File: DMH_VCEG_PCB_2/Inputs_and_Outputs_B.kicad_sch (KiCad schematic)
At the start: 34 parts, among them J11 TS_Jack_6.35mm_Sw, J12 TS_Jack_6.35mm_Sw, J13 TS_Jack_6.35mm_Sw, J14 TS_Jack_6.35mm_Sw, J15 TS_Jack_6.35mm_Sw, J16 TS_Jack_6.35mm_Sw, J17 TS_Jack_6.35mm_Sw, J18 TS_Jack_6.35mm_Sw, J19 TS_Jack_6.35mm_Sw, J20 TS_Jack_6.35mm_Sw, J24 Conn_01x10_PinHeader, J25 Conn_01x10_PinHeader, J26 Conn_01x10_PinHeader, J27 Conn_01x06_PinHeader, U18 TL074, U21 TL072

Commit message: Placed ICs and pin headers on PCB 2
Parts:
- J24, J25, J26: footprint Connector_PinHeader_2.54mm:PinHeader_1x10_P2.54mm_Vertical -> Connector_PinSocket_2.54mm:PinSocket_1x10_P2.54mm_Vertical
- J27: footprint (none) -> Connector_PinSocket_2.54mm:PinSocket_1x06_P2.54mm_Vertical
- U21: footprint Package_DIP:DIP-8_W7.62mm -> Package_DIP:DIP-8_W7.62mm_Socket
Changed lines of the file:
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@@
 			)
 		)
-		(property "Footprint" "Connector_PinHeader_2.54mm:PinHeader_1x10_P2.54mm_Vertical"
+		(property "Footprint" "Connector_PinSocket_2.54mm:PinSocket_1x10_P2.54mm_Vertical"
 			(at 144.78 124.46 0)
 			(effects
@@
 			)
 		)
-		(property "Footprint" "Connector_PinHeader_2.54mm:PinHeader_1x10_P2.54mm_Vertical"
+		(property "Footprint" "Connector_PinSocket_2.54mm:PinSocket_1x10_P2.54mm_Vertical"
 			(at 81.28 26.67 0)
 			(effects
@@
 			)
 		)
-		(property "Footprint" "Connector_PinHeader_2.54mm:PinHeader_1x10_P2.54mm_Vertical"
+		(property "Footprint" "Connector_PinSocket_2.54mm:PinSocket_1x10_P2.54mm_Vertical"
 			(at 190.5 151.13 0)
 			(effects
@@
 			)
 		)
-		(property "Footprint" "Connector_PinHeader_2.54mm:PinHeader_1x10_P2.54mm_Vertical"
+		(property "Footprint" "Connector_PinSocket_2.54mm:PinSocket_1x10_P2.54mm_Vertical"
 			(at 190.5 153.67 0)
 			(effects
@@
 			)
 		)
-		(property "Footprint" ""
+		(property "Footprint" "Connector_PinSocket_2.54mm:PinSocket_1x06_P2.54mm_Vertical"
 			(at 107.95 223.52 0)
 			(effects
@@
 			)
 		)
-		(property "Footprint" "Connector_PinHeader_2.54mm:PinHeader_1x10_P2.54mm_Vertical"
+		(property "Footprint" "Connector_PinSocket_2.54mm:PinSocket_1x10_P2.54mm_Vertical"
 			(at 190.5 166.37 0)
 			(effects
@@
 			)
 		)
-		(property "Footprint" "Connector_PinHeader_2.54mm:PinHeader_1x10_P2.54mm_Vertical"
+		(property "Footprint" "Connector_PinSocket_2.54mm:PinSocket_1x10_P2.54mm_Vertical"
 			(at 190.5 163.83 0)
 			(effects
@@
 			)
 		)
-		(property "Footprint" "Connector_PinHeader_2.54mm:PinHeader_1x10_P2.54mm_Vertical"
+		(property "Footprint" "Connector_PinSocket_2.54mm:PinSocket_1x10_P2.54mm_Vertical"
 			(at 190.5 176.53 0)
 			(effects
@@
 			)
 		)
-		(property "Footprint" ""
+		(property "Footprint" "Connector_PinSocket_2.54mm:PinSocket_1x06_P2.54mm_Vertical"
 			(at 177.8 220.98 0)
 			(effects
@@
 			)
 		)
-		(property "Footprint" "Package_DIP:DIP-8_W7.62mm"
+		(property "Footprint" "Package_DIP:DIP-8_W7.62mm_Socket"
 			(at 146.05 228.6 0)
 			(effects
@@
 			)
 		)
-		(property "Footprint" "Connector_PinHeader_2.54mm:PinHeader_1x10_P2.54mm_Vertical"
+		(property "Footprint" "Connector_PinSocket_2.54mm:PinSocket_1x10_P2.54mm_Vertical"
 			(at 144.78 92.71 0)
 			(effects
@@
 			)
 		)
-		(property "Footprint" "Connector_PinHeader_2.54mm:PinHeader_1x10_P2.54mm_Vertical"
+		(property "Footprint" "Connector_PinSocket_2.54mm:PinSocket_1x10_P2.54mm_Vertical"
 			(at 190.5 179.07 0)
 			(effects
@@
 			)
 		)
-		(property "Footprint" "Connector_PinHeader_2.54mm:PinHeader_1x10_P2.54mm_Vertical"
+		(property "Footprint" "Connector_PinSocket_2.54mm:PinSocket_1x10_P2.54mm_Vertical"
 			(at 81.28 58.42 0)
 			(effects
@@
 			)
 		)
-		(property "Footprint" "Connector_PinHeader_2.54mm:PinHeader_1x10_P2.54mm_Vertical"
+		(property "Footprint" "Connector_PinSocket_2.54mm:PinSocket_1x10_P2.54mm_Vertical"
 			(at 81.28 90.17 0)
 			(effects
@@
 			)
 		)
-		(property "Footprint" "Connector_PinHeader_2.54mm:PinHeader_1x10_P2.54mm_Vertical"
+		(property "Footprint" "Connector_PinSocket_2.54mm:PinSocket_1x10_P2.54mm_Vertical"
 			(at 81.28 119.38 0)
 			(effects
@@
 			)
 		)
-		(property "Footprint" "Connector_PinHeader_2.54mm:PinHeader_1x10_P2.54mm_Vertical"
+		(property "Footprint" "Connector_PinSocket_2.54mm:PinSocket_1x10_P2.54mm_Vertical"
 			(at 144.78 29.21 0)
 			(effects
@@
 			)
 		)
-		(property "Footprint" "Connector_PinHeader_2.54mm:PinHeader_1x10_P2.54mm_Vertical"
+		(property "Footprint" "Connector_PinSocket_2.54mm:PinSocket_1x10_P2.54mm_Vertical"
 			(at 144.78 60.96 0)
 			(effects

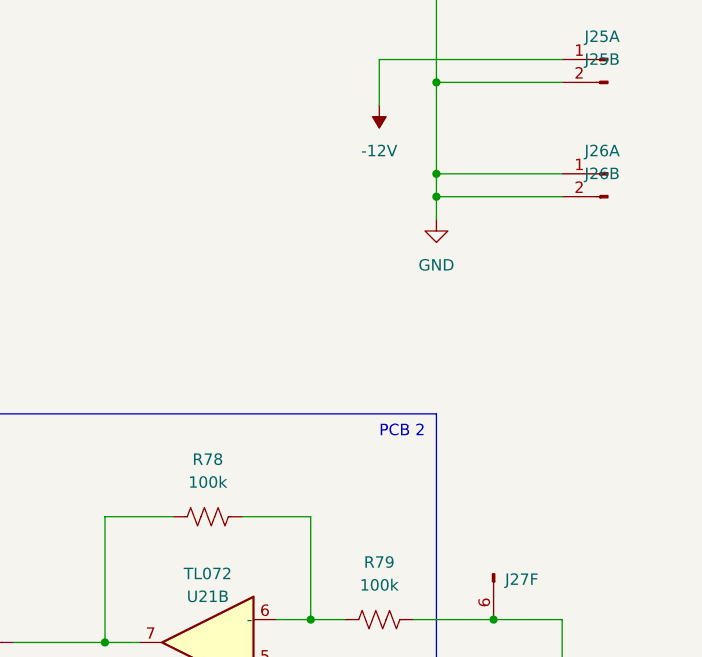
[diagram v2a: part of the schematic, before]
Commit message: Addition of manual gate ongoing
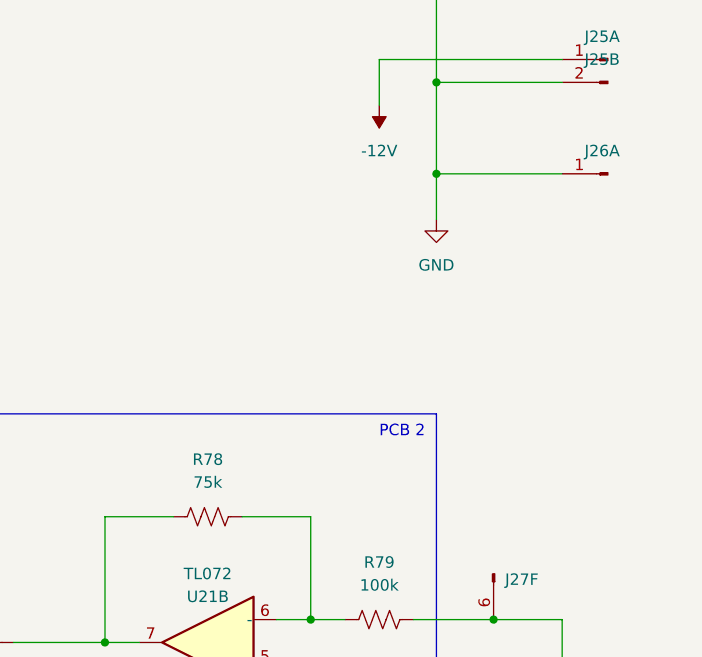
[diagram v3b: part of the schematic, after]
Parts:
- removed unit 2 of J26
- R78: value 100k -> 75k
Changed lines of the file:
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@@
 	)
 	(junction
-		(at 171.45 179.07)
-		(diameter 0)
-		(color 0 0 0 0)
-	)
-	(junction
 		(at 38.1 251.46)
 		(diameter 0)
@@
 	(wire
 		(pts
-			(xy 171.45 179.07) (xy 171.45 181.61)
+			(xy 171.45 176.53) (xy 171.45 181.61)
 		)
 		(stroke
@@
 	(wire
 		(pts
-			(xy 185.42 179.07) (xy 171.45 179.07)
-		)
-		(stroke
-			(width 0)
-			(type default)
-		)
-	)
-	(wire
-		(pts
 			(xy 38.1 99.06) (xy 38.1 124.46)
 		)
@@
 	(wire
 		(pts
-			(xy 171.45 176.53) (xy 171.45 179.07)
-		)
-		(stroke
-			(width 0)
-			(type default)
-		)
-	)
-	(wire
-		(pts
 			(xy 127 110.49) (xy 138.43 110.49)
 		)
@@
 			)
 		)
-		(property "Value" "100k"
+		(property "Value" "75k"
 			(at 146.05 210.82 90)
 			(effects
@@
 				)
 			)
-		)
-	)
-	(symbol
-		(lib_id "SynthStuff:Conn_01x10_PinHeader")
-		(at 190.5 179.07 180)
-		(unit 2)
-		(exclude_from_sim no)
-		(in_bom yes)
-		(on_board yes)
-		(dnp no)
-		(fields_autoplaced yes)
-		(property "Reference" "J26"
-			(at 189.865 176.53 0)
-			(effects
-				(font
-					(size 1.27 1.27)
-				)
-			)
-		)
-		(property "Value" "Conn_01x10_PinHeader"
-			(at 190.5 176.53 0)
-			(effects
-				(font
-					(size 1.27 1.27)
-				)
-				(hide yes)
-			)
-		)
-		(property "Footprint" "Connector_PinSocket_2.54mm:PinSocket_1x10_P2.54mm_Vertical"
-			(at 190.5 179.07 0)
-			(effects
-				(font
-					(size 1.27 1.27)
-				)
-				(hide yes)
-			)
-		)
-		(property "Datasheet" "~"
-			(at 190.5 179.07 0)
-			(effects
-				(font
-					(size 1.27 1.27)
-				)
-				(hide yes)
-			)
-		)
-		(property "Description" "Generic connector, single row, 01x10"
-			(at 190.5 179.07 0)
-			(effects
-				(font
-					(size 1.27 1.27)
-				)
-				(hide yes)
-			)
-		)
-		(pin "6"
-		)
-		(pin "1"
-		)
-		(pin "5"
-		)
-		(pin "4"
-		)
-		(pin "10"
-		)
-		(pin "3"
-		)
-		(pin "2"
-		)
-		(pin "9"
-		)
-		(pin "7"
-		)
-		(pin "8"
-		)
-		(instances
-			(project "DMH_VCEG_PCB_1"
-				(path "/58f4306d-5387-4983-bb08-41a2313fd315/56bd3f35-094b-4adb-8c6d-1e57b38bb61e"
-					(reference "J26")
-					(unit 2)
-				)
-			)

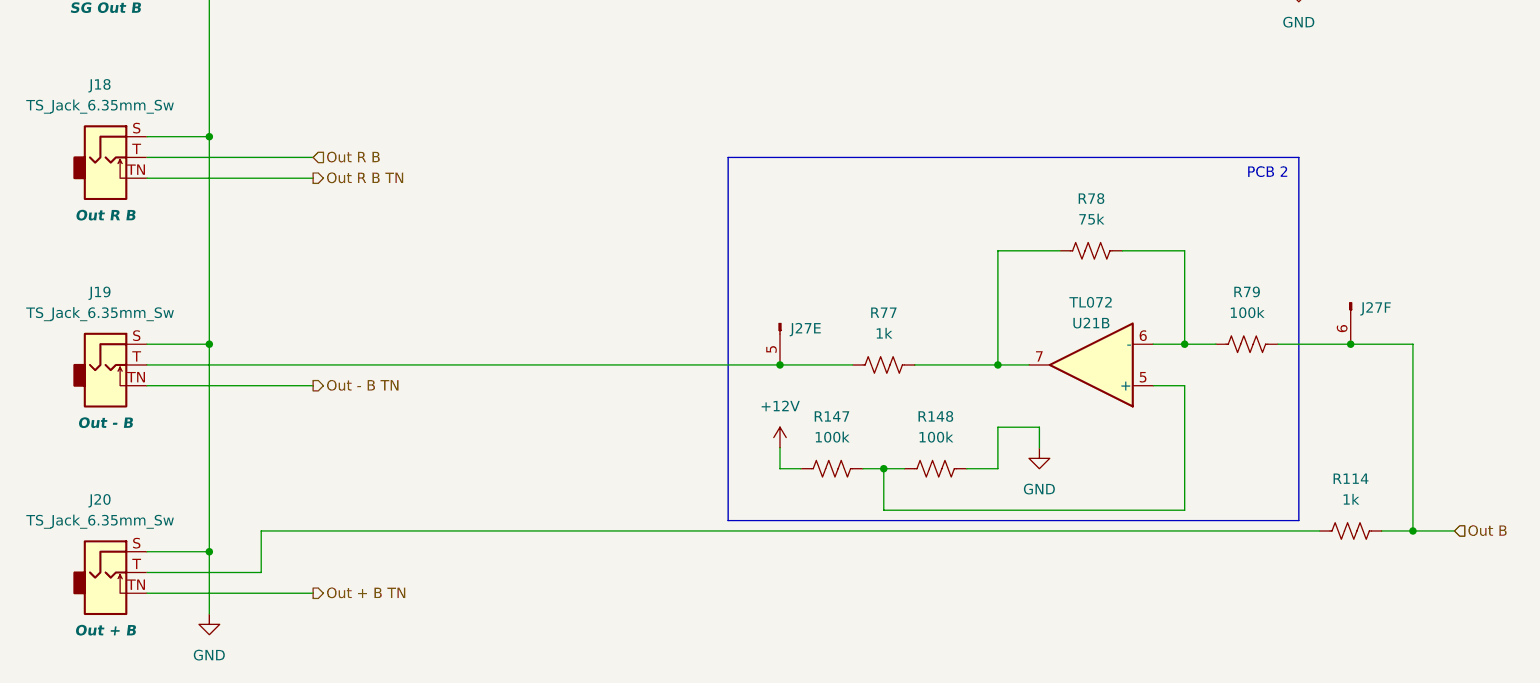
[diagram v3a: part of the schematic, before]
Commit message: Added Output attenuation circuit
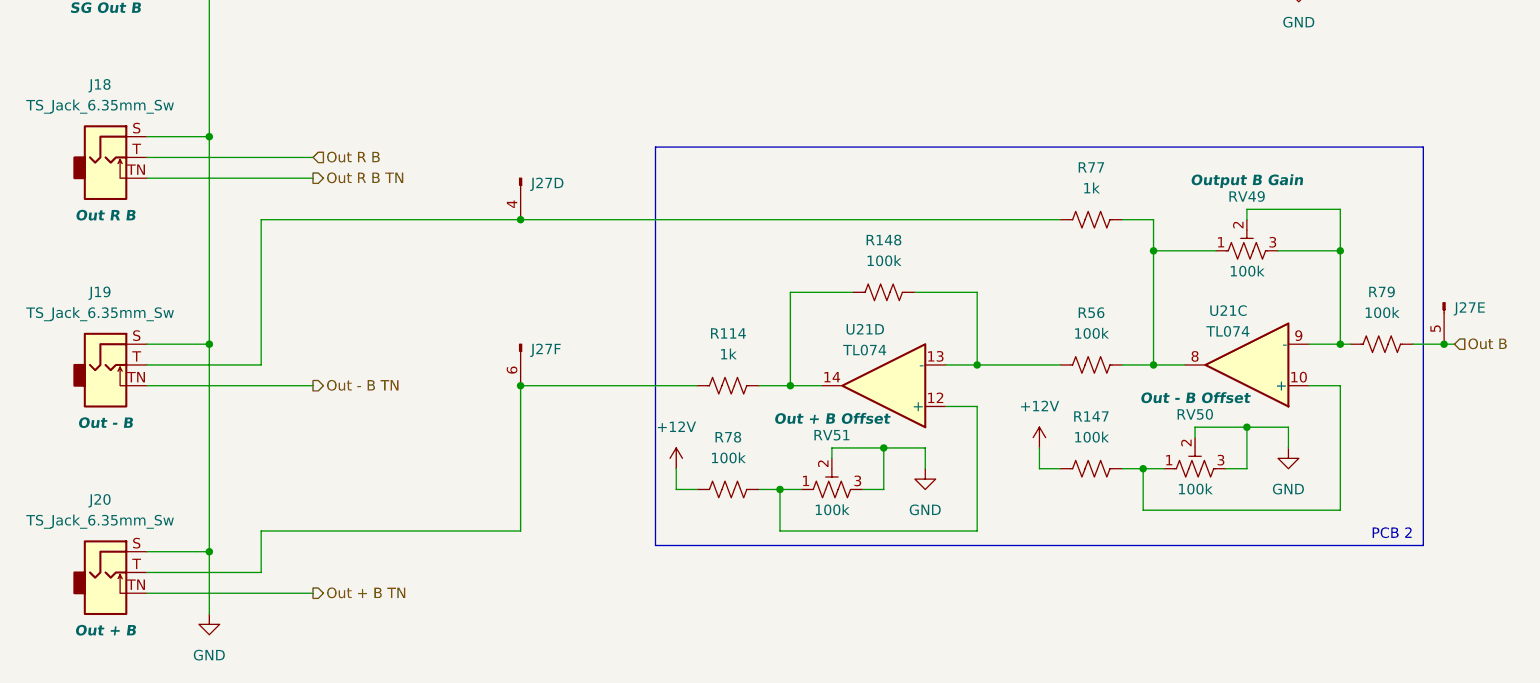
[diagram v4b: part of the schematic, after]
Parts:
- removed U21: TL072, Package_DIP:DIP-8_W7.62mm_Socket, symbol Amplifier_Operational:TL072
- added unit 4 of J27
- added R56: 100k, Resistor_THT:R_Axial_DIN0207_L6.3mm_D2.5mm_P7.62mm_Horizontal, symbol Device:R_US
- added RV49, RV50, RV51: 100k, Potentiometer_THT:Potentiometer_Bourns_3296X_Horizontal, symbol Device:R_Potentiometer_Trim_US
- added U21: TL074, symbol Amplifier_Operational:TL074
- R78: value 75k -> 100k
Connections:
- net +12V: now also R78.2
- net GND: now also RV50.2, RV50.3, RV51.2, RV51.3; no longer R148.1
- net Out B: now also J27.5 (Pin_5); no longer J27.6 (Pin_6), R114.1
- net at R148.2: now also R114.1, U21.14; no longer R147.1
- net at J19.T, R77.2: now also J27.4 (Pin_4); no longer J27.5 (Pin_5)
- net at R78.1: now also RV51.1, U21.12 (+); no longer R79.2
- net at R77.1: now also R56.1, RV49.1, U21.8; no longer R78.2
- net at J20.T, R114.2: now also J27.6 (Pin_6)
- new net: R148.1, R56.2, U21.13 (-)
- new net: R147.1, RV50.1, U21.10 (+)
- new net: R79.2, RV49.2, RV49.3, U21.9 (-)
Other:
- moved on the sheet: R114, R147, R148, R77, R79
